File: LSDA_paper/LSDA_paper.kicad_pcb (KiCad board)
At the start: 2 copper layers, 81 parts, among them Q1 BC547, Q2 BC547, U1 LM324

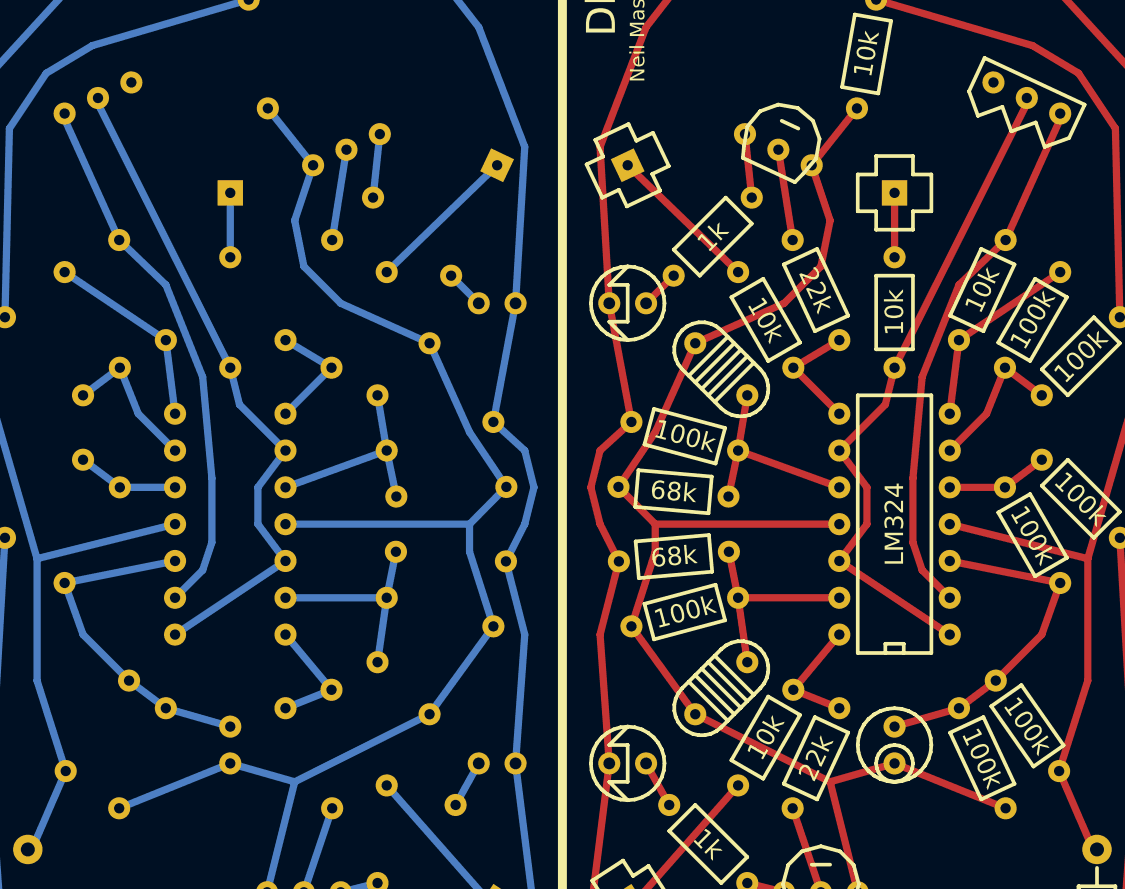
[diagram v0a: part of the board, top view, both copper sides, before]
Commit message: Updated LED footprints - thanks Josh
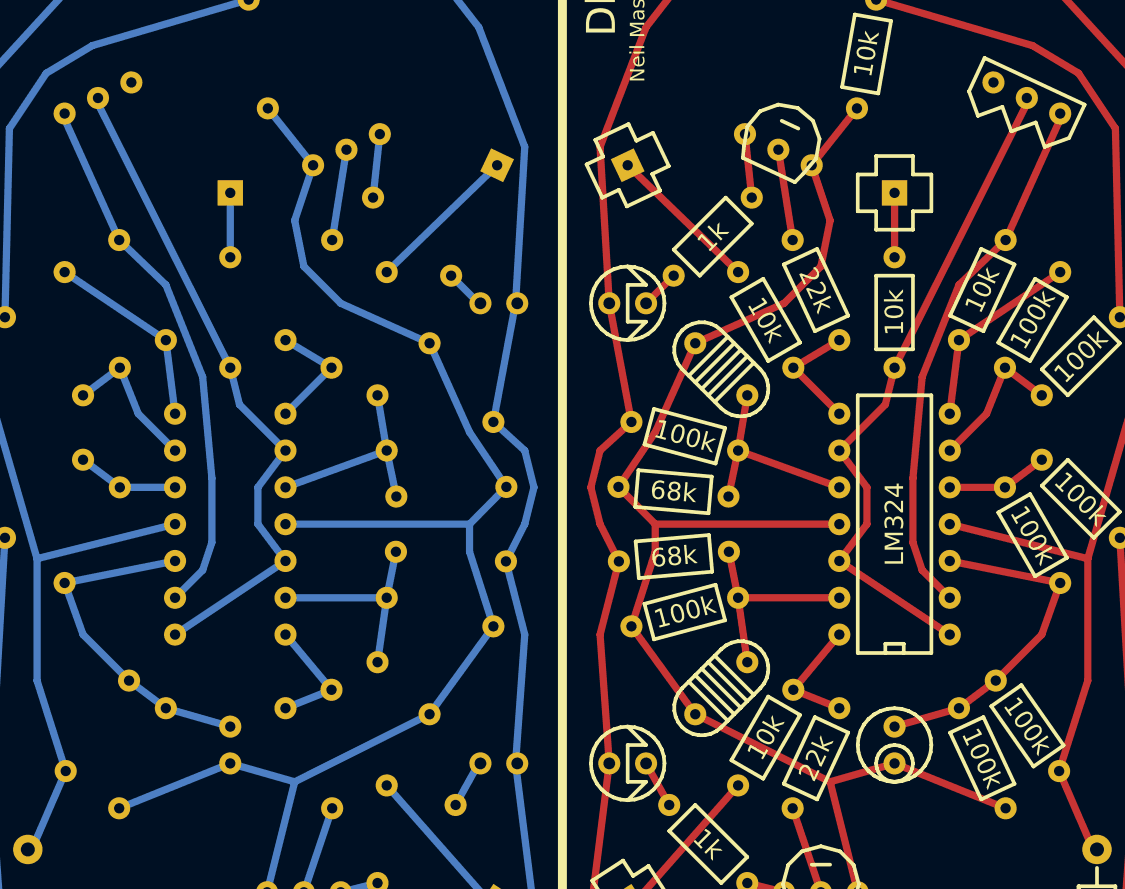
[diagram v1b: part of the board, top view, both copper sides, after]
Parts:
- moved D1 2.54 mm to (65.4, 85.1), turned to 180 degrees
- moved D2 2.54 mm to (65.4, 116.8), turned to 180 degrees
- moved D1 2.42 mm to (54.0, 85.1), turned to 0 degrees
- moved D2 2.42 mm to (54.0, 116.8), turned to 0 degrees
